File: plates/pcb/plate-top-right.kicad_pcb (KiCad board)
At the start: 2 copper layers, 124.7 x 92.2 mm, 0 parts

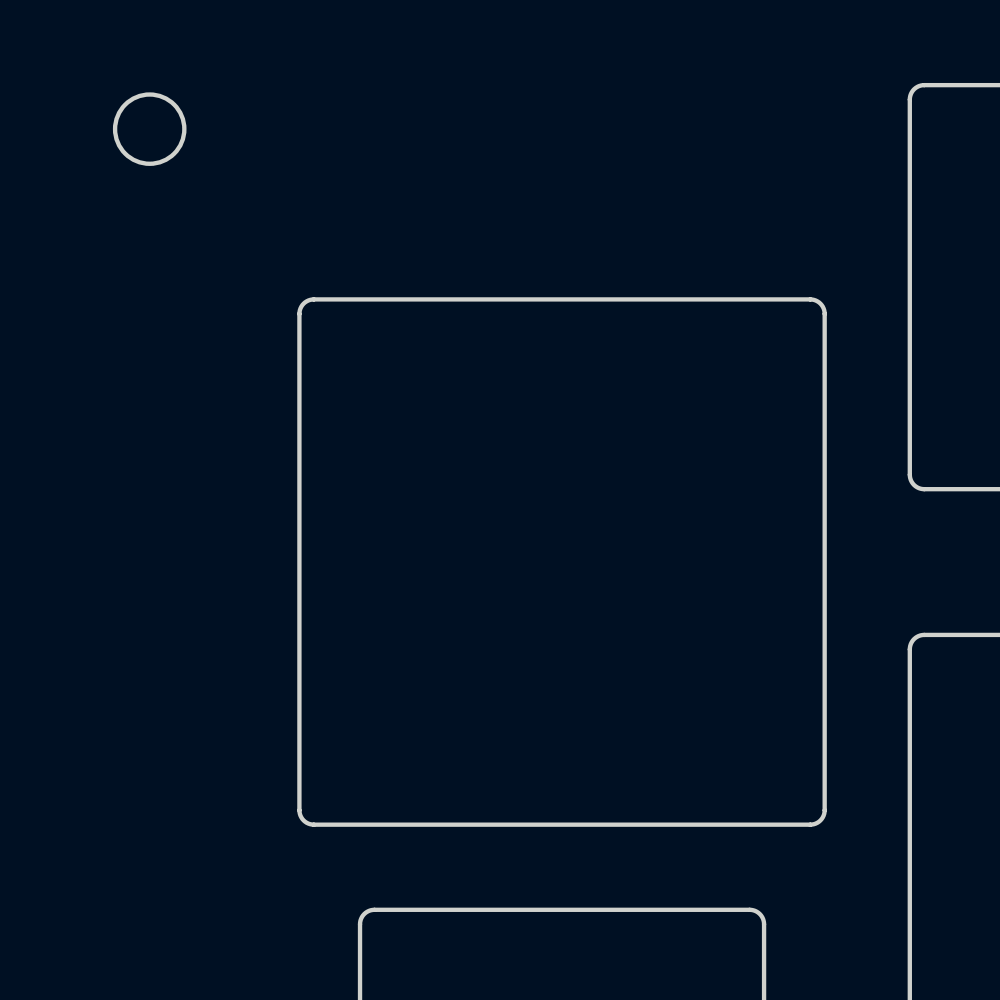
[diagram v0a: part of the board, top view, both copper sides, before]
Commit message: feat(pcb): integrate sunk inertia wheel cutout and rJ5 connector into curcur40-right and top plate
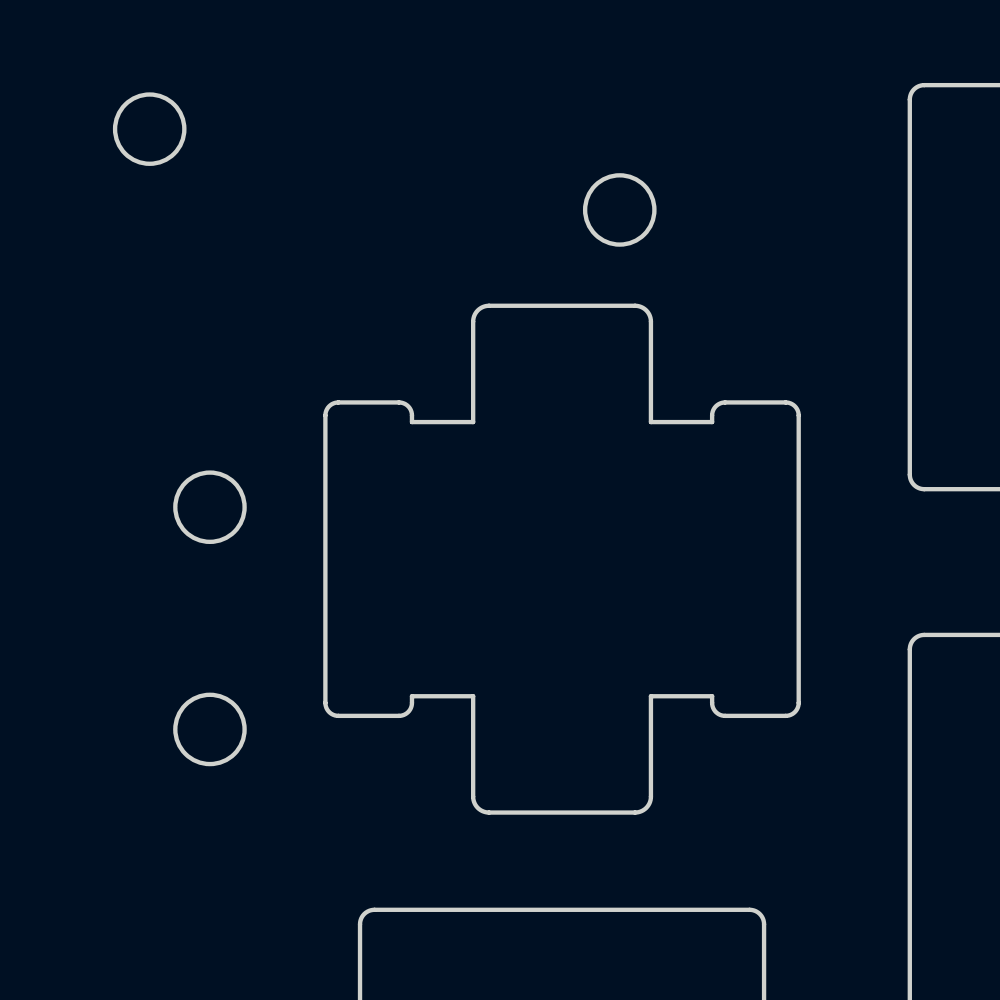
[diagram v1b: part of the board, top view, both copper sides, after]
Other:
- outline, holes or cut-outs redrawn
